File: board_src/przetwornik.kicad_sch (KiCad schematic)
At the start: 4 parts, among them IC5 MCP3202-CI_MS, J23 Conn_01x04, J4 Conn_01x04

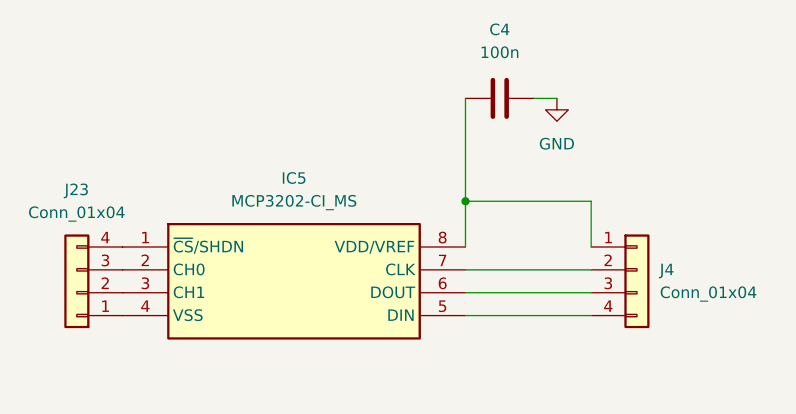
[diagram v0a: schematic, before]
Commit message: dodany tranzystor BS123
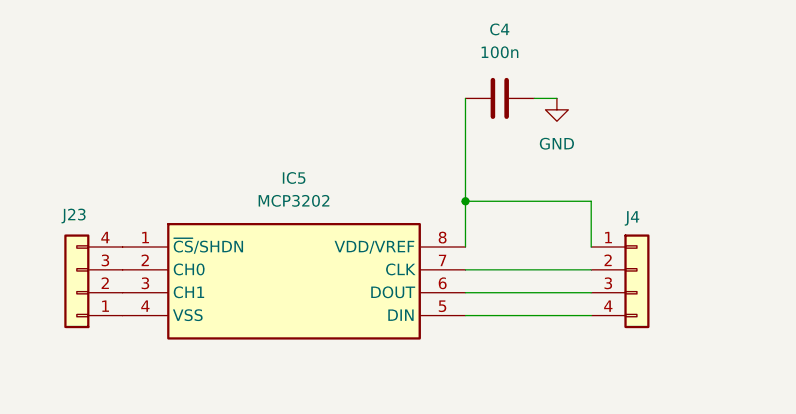
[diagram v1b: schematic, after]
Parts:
- IC5: value MCP3202-CI_MS -> MCP3202; footprint footprints:SOP65P490X110-8N -> Package_SO:SOIC-8_5.3x5.3mm_P1.27mm
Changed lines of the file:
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@@
 		(on_board yes)
 		(dnp no)
-		(fields_autoplaced yes)
 		(property "Reference" "J4"
-			(at 137.16 83.8199 0)
+			(at 133.35 77.978 0)
 			(effects
 				(font
@@
 				)
 				(justify left)
+				(hide yes)
 			)
 		)
@@
 		(on_board yes)
 		(dnp no)
-		(fields_autoplaced yes)
 		(property "Reference" "J23"
-			(at 72.39 74.93 0)
+			(at 72.136 77.724 0)
 			(effects
 				(font
@@
 					(size 1.27 1.27)
 				)
+				(hide yes)
 			)
 		)
@@
 			)
 		)
-		(property "Value" "MCP3202-CI_MS"
+		(property "Value" "MCP3202"
 			(at 96.52 76.2 0)
 			(effects
@@
 			)
 		)
-		(property "Footprint" "footprints:SOP65P490X110-8N"
+		(property "Footprint" "Package_SO:SOIC-8_5.3x5.3mm_P1.27mm"
 			(at 111.76 176.2 0)
 			(effects

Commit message: Poprawki w schematach. Rozpoczęte korekty płytki
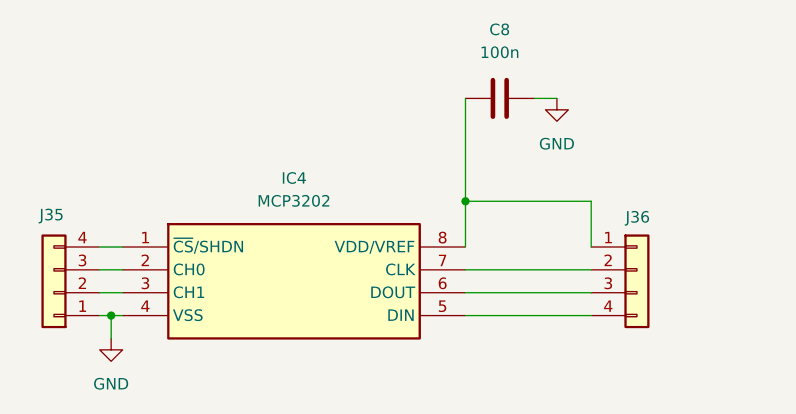
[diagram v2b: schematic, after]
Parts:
- C8: renamed from C4; footprint Capacitor_SMD:C_0603_1608Metric -> Capacitor_SMD:C_0603_1608Metric_Pad1.08x0.95mm_HandSolder
- IC4: renamed from IC5; footprint Package_SO:SOIC-8_5.3x5.3mm_P1.27mm -> footprints:SOP65P780X200-28N
- J35: renamed from J23; footprint Connector_PinHeader_2.54mm:PinHeader_1x04_P2.54mm_Vertical -> Connector_PinHeader_2.54mm:PinHeader_1x02_P2.54mm_Vertical
- J36: renamed from J4; footprint Connector_PinHeader_2.54mm:PinHeader_1x04_P2.54mm_Vertical -> Connector_PinSocket_2.54mm:PinSocket_1x20_P2.54mm_Vertical
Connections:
- net GND: now also IC4.4 (VSS), J35.1 (Pin_1)
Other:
- moved on the sheet: J35
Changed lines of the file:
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@@
 		(color 0 0 0 0)
 	)
+	(junction
+		(at 76.2 88.9)
+		(diameter 0)
+		(color 0 0 0 0)
+	)
+	(wire
+		(pts
+			(xy 76.2 88.9) (xy 77.47 88.9)
+		)
+		(stroke
+			(width 0)
+			(type default)
+		)
+	)
 	(wire
 		(pts
@@
 	(wire
 		(pts
+			(xy 74.93 81.28) (xy 77.47 81.28)
+		)
+		(stroke
+			(width 0)
+			(type default)
+		)
+	)
+	(wire
+		(pts
 			(xy 123.19 64.77) (xy 125.73 64.77)
 		)
@@
 	(wire
 		(pts
+			(xy 74.93 88.9) (xy 76.2 88.9)
+		)
+		(stroke
+			(width 0)
+			(type default)
+		)
+	)
+	(wire
+		(pts
+			(xy 74.93 86.36) (xy 77.47 86.36)
+		)
+		(stroke
+			(width 0)
+			(type default)
+		)
+	)
+	(wire
+		(pts
 			(xy 129.54 83.82) (xy 115.57 83.82)
+		)
+		(stroke
+			(width 0)
+			(type default)
+		)
+	)
+	(wire
+		(pts
+			(xy 74.93 83.82) (xy 77.47 83.82)
+		)
+		(stroke
+			(width 0)
+			(type default)
+		)
+	)
+	(wire
+		(pts
+			(xy 76.2 88.9) (xy 76.2 91.44)
 		)
 		(stroke
@@
 		(on_board yes)
 		(dnp no)
-		(property "Reference" "J4"
+		(property "Reference" "J36"
 			(at 133.35 77.978 0)
 			(effects
@@
 			)
 		)
-		(property "Footprint" "Connector_PinHeader_2.54mm:PinHeader_1x04_P2.54mm_Vertical"
+		(property "Footprint" "Connector_PinSocket_2.54mm:PinSocket_1x20_P2.54mm_Vertical"
 			(at 134.62 83.82 0)
 			(effects
@@
 			(project ""
 				(path "/772e9f49-cfcf-4cf6-843d-0684684f2d4b/72381f9f-0261-4c9d-a878-5b854177e01f"
-					(reference "J4")
+					(reference "J36")
 					(unit 1)
 				)
@@
 		(dnp no)
 		(fields_autoplaced yes)
-		(property "Reference" "#PWR041"
+		(property "Reference" "#PWR070"
 			(at 125.73 71.12 0)
 			(effects
@@
 			(project ""
 				(path "/772e9f49-cfcf-4cf6-843d-0684684f2d4b/72381f9f-0261-4c9d-a878-5b854177e01f"
-					(reference "#PWR041")
+					(reference "#PWR070")
 					(unit 1)
 				)
@@
 		(dnp no)
 		(fields_autoplaced yes)
-		(property "Reference" "C4"
+		(property "Reference" "C8"
 			(at 119.38 57.15 90)
 			(effects
@@
 			)
 		)
-		(property "Footprint" "Capacitor_SMD:C_0603_1608Metric"
+		(property "Footprint" "Capacitor_SMD:C_0603_1608Metric_Pad1.08x0.95mm_HandSolder"
 			(at 123.19 63.8048 0)
 			(effects
@@
 			(project ""
 				(path "/772e9f49-cfcf-4cf6-843d-0684684f2d4b/72381f9f-0261-4c9d-a878-5b854177e01f"
-					(reference "C4")
+					(reference "C8")
 					(unit 1)
 				)
@@
 	(symbol
 		(lib_id "Connector_Generic:Conn_01x04")
-		(at 72.39 86.36 180)
+		(at 69.85 86.36 180)
 		(unit 1)
 		(exclude_from_sim no)
@@
 		(on_board yes)
 		(dnp no)
-		(property "Reference" "J23"
-			(at 72.136 77.724 0)
+		(property "Reference" "J35"
+			(at 69.596 77.724 0)
 			(effects
 				(font
@@
 		)
 		(property "Value" "Conn_01x04"
-			(at 72.39 77.47 0)
-			(effects
-				(font
-					(size 1.27 1.27)
-				)
-				(hide yes)
-			)
-		)
-		(property "Footprint" "Connector_PinHeader_2.54mm:PinHeader_1x04_P2.54mm_Vertical"
-			(at 72.39 86.36 0)
+			(at 69.85 77.47 0)
+			(effects
+				(font
+					(size 1.27 1.27)
+				)
+				(hide yes)
+			)
+		)
+		(property "Footprint" "Connector_PinHeader_2.54mm:PinHeader_1x02_P2.54mm_Vertical"
+			(at 69.85 86.36 0)
 			(effects
 				(font
@@
 		)
 		(property "Datasheet" "~"
-			(at 72.39 86.36 0)
+			(at 69.85 86.36 0)
 			(effects
 				(font
@@
 		)
 		(property "Description" "Generic connector, single row, 01x04, script generated (kicad-library-utils/schlib/autogen/connector/)"
-			(at 72.39 86.36 0)
+			(at 69.85 86.36 0)
 			(effects
 				(font
@@
 			(project "board"
 				(path "/772e9f49-cfcf-4cf6-843d-0684684f2d4b/72381f9f-0261-4c9d-a878-5b854177e01f"
-					(reference "J23")
+					(reference "J35")
 					(unit 1)
 				)
@@
 		(dnp no)
 		(fields_autoplaced yes)
-		(property "Reference" "IC5"
+		(property "Reference" "IC4"
 			(at 96.52 73.66 0)
 			(effects
@@
 			)
 		)
-		(property "Footprint" "Package_SO:SOIC-8_5.3x5.3mm_P1.27mm"
+		(property "Footprint" "footprints:SOP65P780X200-28N"
 			(at 111.76 176.2 0)
 			(effects
@@
 			(project "board"
 				(path "/772e9f49-cfcf-4cf6-843d-0684684f2d4b/72381f9f-0261-4c9d-a878-5b854177e01f"
-					(reference "IC5")
+					(reference "IC4")
 					(unit 1)
 				)
+			)
+		)
+	)
+	(symbol
+		(lib_id "power:GND")
+		(at 76.2 91.44 0)
+		(unit 1)
+		(exclude_from_sim no)
+		(in_bom yes)
+		(on_board yes)
+		(dnp no)
+		(fields_autoplaced yes)
+		(property "Reference" "#PWR069"
+			(at 76.2 97.79 0)
+			(effects
+				(font
+					(size 1.27 1.27)
+				)
+				(hide yes)
+			)
+		)
+		(property "Value" "GND"
+			(at 76.2 96.52 0)
+			(effects
+				(font
+					(size 1.27 1.27)
+				)
+			)
+		)
+		(property "Footprint" ""
+			(at 76.2 91.44 0)
+			(effects
+				(font
+					(size 1.27 1.27)
+				)
+				(hide yes)
+			)
+		)
+		(property "Datasheet" ""
+			(at 76.2 91.44 0)
+			(effects
+				(font
+					(size 1.27 1.27)
+				)
+				(hide yes)
+			)
+		)
+		(property "Description" "Power symbol creates a global label with name \"GND\" , ground"
+			(at 76.2 91.44 0)
+			(effects
+				(font
+					(size 1.27 1.27)
+				)
+				(hide yes)
+			)
+		)
+		(pin "1"
+		)
+		(instances
+			(project "board"
+				(path "/772e9f49-cfcf-4cf6-843d-0684684f2d4b/72381f9f-0261-4c9d-a878-5b854177e01f"
+					(reference "#PWR069")
+					(unit 1)
+				)

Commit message: Naniesione poprawki na projekcie płytki. Wersja końcowa
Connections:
- net GND: now also J35.4 (Pin_4); no longer J35.1 (Pin_1)
- net at J35.2 (Pin_2): now also IC4.2 (CH0); no longer IC4.3 (CH1)
- net at J35.3 (Pin_3): now also IC4.3 (CH1); no longer IC4.2 (CH0)
- net at IC4.1 (~{CS}/SHDN): now also J35.1 (Pin_1); no longer J35.4 (Pin_4)
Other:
- moved on the sheet: J35
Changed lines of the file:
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@@
 	(symbol
 		(lib_id "Connector_Generic:Conn_01x04")
-		(at 69.85 86.36 180)
+		(at 69.85 83.82 0)
+		(mirror y)
 		(unit 1)
 		(exclude_from_sim no)
@@
 		(dnp no)
 		(property "Reference" "J35"
-			(at 69.596 77.724 0)
+			(at 69.596 92.456 0)
 			(effects
 				(font
@@
 		)
 		(property "Value" "Conn_01x04"
-			(at 69.85 77.47 0)
+			(at 69.85 92.71 0)
 			(effects
 				(font
@@
 		)
 		(property "Footprint" "Connector_PinHeader_2.54mm:PinHeader_1x02_P2.54mm_Vertical"
-			(at 69.85 86.36 0)
+			(at 69.85 83.82 0)
 			(effects
 				(font
@@
 		)
 		(property "Datasheet" "~"
-			(at 69.85 86.36 0)
+			(at 69.85 83.82 0)
 			(effects
 				(font
@@
 		)
 		(property "Description" "Generic connector, single row, 01x04, script generated (kicad-library-utils/schlib/autogen/connector/)"
-			(at 69.85 86.36 0)
+			(at 69.85 83.82 0)
 			(effects
 				(font

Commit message: Wprowadzono usprawnienia i poprawki. Wersja ostateczna, wysłana do JLCPCB.
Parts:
- IC4: footprint footprints:SOP65P780X200-28N -> Package_DIP:DIP-8_W7.62mm_Socket_LongPads
- J35: footprint Connector_PinHeader_2.54mm:PinHeader_1x02_P2.54mm_Vertical -> Connector_PinHeader_2.54mm:PinHeader_1x04_P2.54mm_Vertical
- J36: footprint Connector_PinSocket_2.54mm:PinSocket_1x20_P2.54mm_Vertical -> Connector_PinHeader_2.54mm:PinHeader_1x04_P2.54mm_Vertical
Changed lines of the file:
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@@
 			)
 		)
-		(property "Footprint" "Connector_PinSocket_2.54mm:PinSocket_1x20_P2.54mm_Vertical"
+		(property "Footprint" "Connector_PinHeader_2.54mm:PinHeader_1x04_P2.54mm_Vertical"
 			(at 134.62 83.82 0)
 			(effects
@@
 			)
 		)
-		(property "Footprint" "Connector_PinHeader_2.54mm:PinHeader_1x02_P2.54mm_Vertical"
+		(property "Footprint" "Connector_PinHeader_2.54mm:PinHeader_1x04_P2.54mm_Vertical"
 			(at 69.85 83.82 0)
 			(effects
@@
 			)
 		)
-		(property "Footprint" "footprints:SOP65P780X200-28N"
+		(property "Footprint" "Package_DIP:DIP-8_W7.62mm_Socket_LongPads"
 			(at 111.76 176.2 0)
 			(effects
